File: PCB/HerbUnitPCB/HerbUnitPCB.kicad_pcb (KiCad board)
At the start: 2 copper layers, 57.4 x 61.5 mm, 48 parts, among them J1 USB_C_Receptacle_USB2.0_16P, J2 Barrel_Jack_Switch_Pin3Ring, J3 Conn_01x03_Pin, J4 SD_Card_Device, J5 Screw_Terminal_01x02, J6 Conn_01x03_Pin, SW1 SW_Push, SW2 SW_Push, SW3 SW_Push, U1 USBLC6-2P6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

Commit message: New Gerber
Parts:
- removed the G*** at (184.0, 89.6)
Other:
- board text added: "PROJECT HERBINATOR"

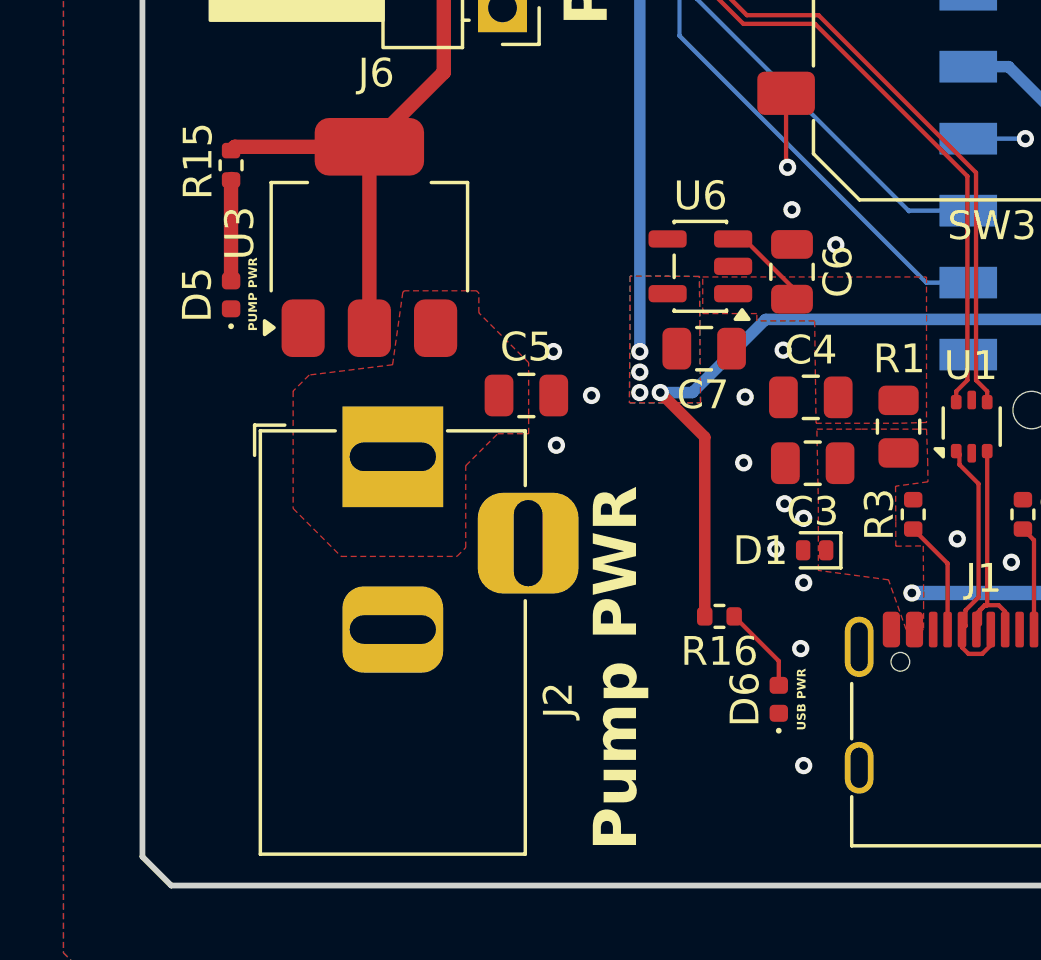
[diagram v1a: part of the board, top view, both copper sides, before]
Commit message: Updated BOM to have all parts.
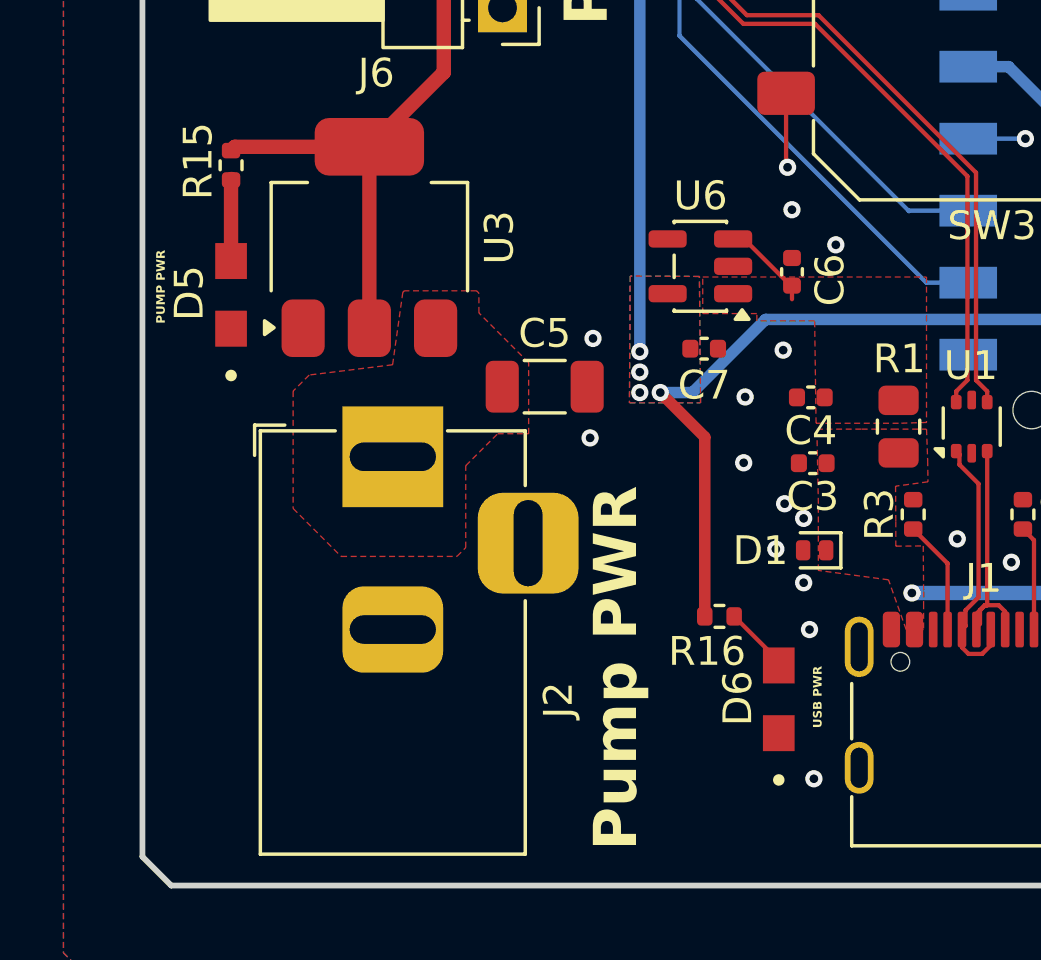
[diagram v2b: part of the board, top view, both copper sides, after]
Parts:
- C3, C4, C6, C7: footprint Capacitor_SMD:C_0805_2012Metric -> Capacitor_SMD:C_0402_1005Metric
- C5: footprint Capacitor_SMD:C_0805_2012Metric -> Capacitor_SMD:C_1206_3216Metric
- D5, D6: footprint LED_SMD:LED_0402_1005Metric -> GreenLED:LED_APT2012CGCK
- R1: value 0 -> 330
- SW1, SW2: value SW_Push -> BootButtons
- SW3: value SW_Push -> CalibrationButton
- moved C5 0.71 mm to (151.9, 78.7)
- moved G*** 0.61 mm to (167.8, 46.5)
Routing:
- net Net-(D6-A): track 3.06 -> 2.21 mm
- net Net-(D5-A): track 3.55 -> 2.86 mm
- net GND: vias 37 -> 36
